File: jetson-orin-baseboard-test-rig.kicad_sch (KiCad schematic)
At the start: 18 parts, among them J1 PinHeader_2x6_P2.54mm_Drill1.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, J2 PinHeader_2x6_P2.54mm_Drill1.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, J3 PinHeader_2x6_P2.54mm_Drill1.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, J4 PinHeader_2x6_P2.54mm_Drill1.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, J5 PinHeader_2x6_P2.54mm_Drill1.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, J6 PinHeader_2x6_P2.54mm_Drill1.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, J7 PinHeader_2x6_P2.54mm_Drill1.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

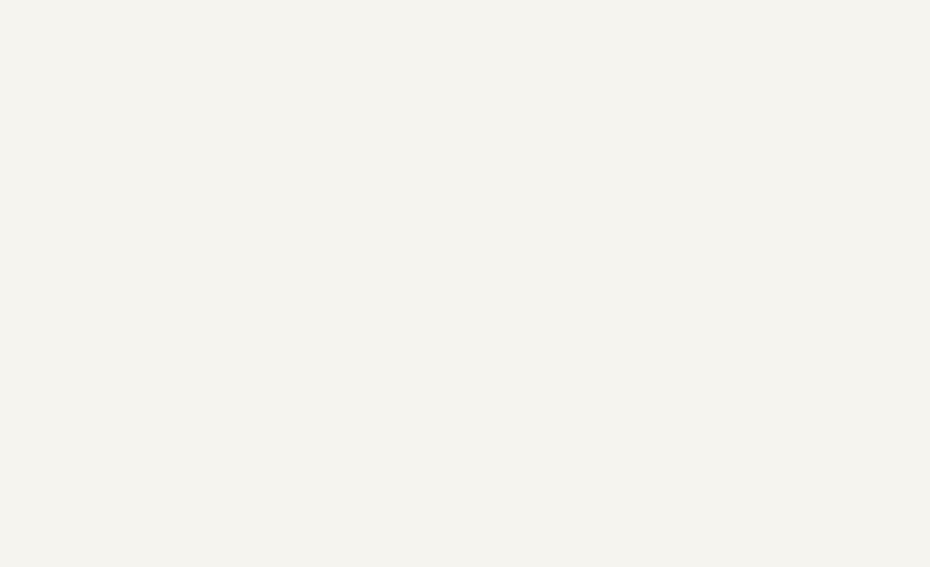
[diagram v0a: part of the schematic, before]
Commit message: [#77400] Add spring probes (WiP)
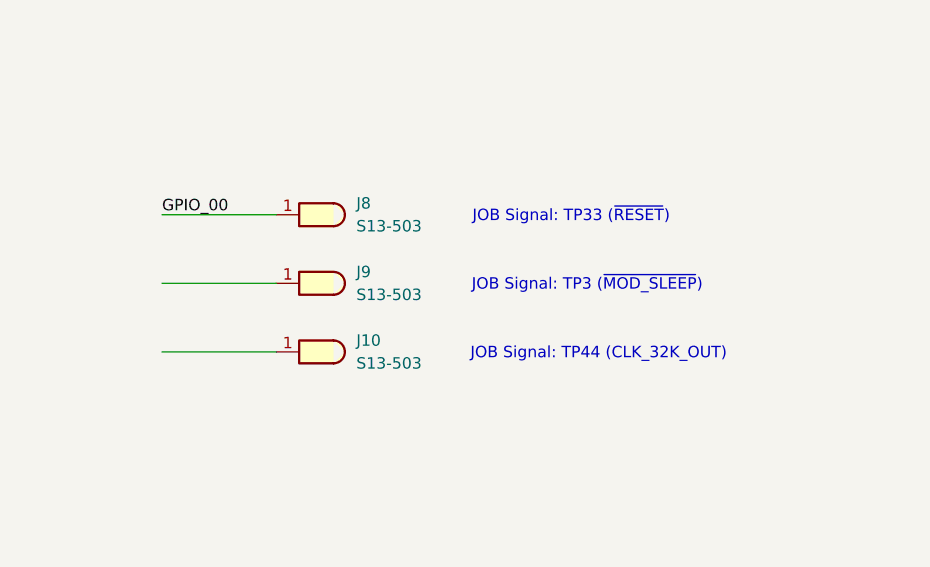
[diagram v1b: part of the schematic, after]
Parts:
- added J10, J8, J9: Harwin_1x1_H17.75mm_Drill0.8mm_S13-503, antmicro-footprints:PogoPin_Harwin_1x1_H17.75mm_Drill0.8mm_S13-503, symbol antmicroPogoPins:Harwin_1x1_H17.75mm_Drill0.8mm_S13-503
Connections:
- net GPIO_00: now also J8.1
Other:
- note added: "JOB Signal: TP3 (~{MOD_SLEEP})"
- note added: "JOB Signal: TP33 (~{RESET})"
- note added: "JOB Signal: TP44 (CLK_32K_OUT)"

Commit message: [#77400] Finalize schematic
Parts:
- added D1, D2: LED_G_0603_KP-1608CGCK, antmicro-footprints:LED_0603_1608Metric_G, symbol antmicroLEDIndicationDiscrete:LED_G_0603_KP-1608CGCK
- added J11, J12, J13, J14, J15, J16, J17, J18, J19, J20, J21, J22, J23, J24, J25, J26, J27, J28, J29, J30: Harwin_1x1_H17.75mm_Drill0.8mm_S13-503, antmicro-footprints:PogoPin_Harwin_1x1_H17.75mm_Drill0.8mm_S13-503, symbol antmicroPogoPins:Harwin_1x1_H17.75mm_Drill0.8mm_S13-503
- added Q1: BSS84, antmicro-footprints:SOT-23-3, symbol antmicroTransistorsFETsMOSFETsSingle:BSS84
- added R1: R_330R_0402, antmicro-footprints:R_0402_1005Metric, symbol antmicroResistors0402:R_330R_0402
- added R10, R11, R12, R18, R3, R5, R6, R7, R8, R9: R_0R_0402, antmicro-footprints:R_0402_1005Metric, symbol antmicroResistors0402:R_0R_0402
- added R13, R2: R_3k9_0402, antmicro-footprints:R_0402_1005Metric, symbol antmicroResistors0402:R_3k9_0402
- added R14, R15, R16, R17: R_68k_0402, antmicro-footprints:R_0402_1005Metric, symbol antmicroResistors0402:R_68k_0402
- added R19, R4: R_10k_0402, antmicro-footprints:R_0402_1005Metric, symbol antmicroResistors0402:R_10k_0402
- H3, H4, H5, H6: now not fitted; now left out of the parts list
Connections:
- net +3V3: now also D1.2 (A), Q1.2 (S), R19.2, R4.2
- net ADC_A_IN0: now also R17.1
- net ADC_A_IN1: now also R16.1
- net ADC_A_IN2: now also R15.1
- net ADC_A_IN3: now also R14.1
- net ADC_A_IN4: now also R13.2
- net ADC_A_IN5: now also R10.1
- net ADC_A_IN6: now also R11.1
- net ADC_A_IN7: now also R12.1
- net GND: now also J24.1, R1.1, R2.1
- net GPIO_00: now also R3.1; no longer J8.1
- net GPIO_01: now also R18.1, R19.1, R9.1
- net SPI_CS0: now also R5.1
- net SPI_MISO: now also R7.1
- net SPI_MOSI: now also R8.1
- net SPI_SCLK: now also R6.1
- net VCC: now also D2.2 (A)
- new net: J27.1, R6.2
- new net: D2.1 (C), R2.2
- new net: J23.1, R12.2
- new net: J19.1, R14.2
- new net: J22.1, R11.2
- new net: J21.1, R10.2
- new net: J18.1, R15.2
- new net: J28.1, R7.2
- new net: J16.1, R17.2
- new net: J20.1, R13.1
- new net: J8.1, R3.2
- new net: J25.1, Q1.3 (D)
- new net: D1.1 (C), R1.2
- new net: J26.1, R5.2
- new net: Q1.1 (G), R4.1, R9.2
- new net: J29.1, R8.2
- new net: J17.1, R16.2
- new net: J30.1, R18.2
- no-connect marks 0 -> 7
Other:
- note added: "Analog: 0-1.8V"
- note added: "Analog: 0-20V"
- note added: "Analog: 0-3.3V"
- note added: "Analog: 0-5V"
- note added: "Input on JOB (3V3): * Drive high to turn on +5V, +3V3 and +1V8 power rails * Keep HiZ otherwise"
- note added: "JOB Signal: J9-Pin1 (EEPROM_PWR)"
- note added: "JOB Signal: J9-Pin2 (~{CS})"
- note added: "JOB Signal: J9-Pin4 (SCK)"
- note added: "JOB Signal: J9-Pin6 (MISO)"
- note added: "JOB Signal: J9-Pin8 (MOSI)"
- note added: "JOB Signal: SP7-Pin1 (GND)"
- note added: "JOB Signal: TP1 (USBC3_VBUS)"
- note added: "JOB Signal: TP13 (U6-Pin30)"
- note added: "JOB Signal: TP14 (VCC)"
- note added: "JOB Signal: TP17 (USBC0_VBUS)"
- note added: "JOB Signal: TP22 (HDMI_HPD)"
- note added: "JOB Signal: TP23 (GND)"
- note added: "JOB Signal: TP29 (USBC1_VBUS)"
- note added: "JOB Signal: TP30 (USBC_HPD)"
- note added: "JOB Signal: TP31 (USBC1_DIR)"
- note added: "JOB Signal: TP32 (USBC1_FAULT_N)"
- note added: "JOB Signal: TP52 (3V3_STDB)"
- note added: "JOB Signal: TP53 (+5V)"
- note added: "JOB Signal: TP54 (+3V3)"
- note added: "JOB Signal: TP55 (+1V8)"
- note added: "Set to 0V to turn on EEPROM power Set to HiZ to turn off EEPROM power"
- note added: "This signal can be used to detect presence of the DUT * 0V - DUT is present * 3.3V - DUT is not present"
- moved on the sheet: C1, C2, C3, C4, C5, C6, C7, J1, J2, J3, J4, J5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

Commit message: [#77400] Clean ERC
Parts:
- J10, J11, J12, J13, J14, J15, J16, J17, J18, J19, J20, J21, J22, J23, J24, J25, J26, J27, J28, J29, J30, J8, J9: symbol antmicroPogoPins:Harwin_1x1_H17.75mm_Drill0.8mm_S13-503 -> antmicroPogoPins:Harwin_1x1_H17.75mm_Drill0.8mm_S13-503_CUSTOM
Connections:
- no-connect marks 7 -> 49

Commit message: [#77400] Finish routing
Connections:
- net ADC_A_IN1: now also R15.1; no longer R16.1
- net ADC_A_IN2: now also R13.2; no longer R15.1
- net ADC_A_IN3: now also R11.1; no longer R14.1
- net ADC_A_IN4: now also R16.1; no longer R13.2
- net ADC_A_IN5: now also R14.1; no longer R10.1
- net ADC_A_IN6: now also R10.1; no longer R11.1
- net GPIO_01: no longer R9.1
- net GPIO_02: now also R9.1
- net VCC: now also J19.1, R14.2
- no-connect marks 49 -> 48
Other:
- moved on the sheet: R10, R11, R12, R13, R14, R15, R16, R17

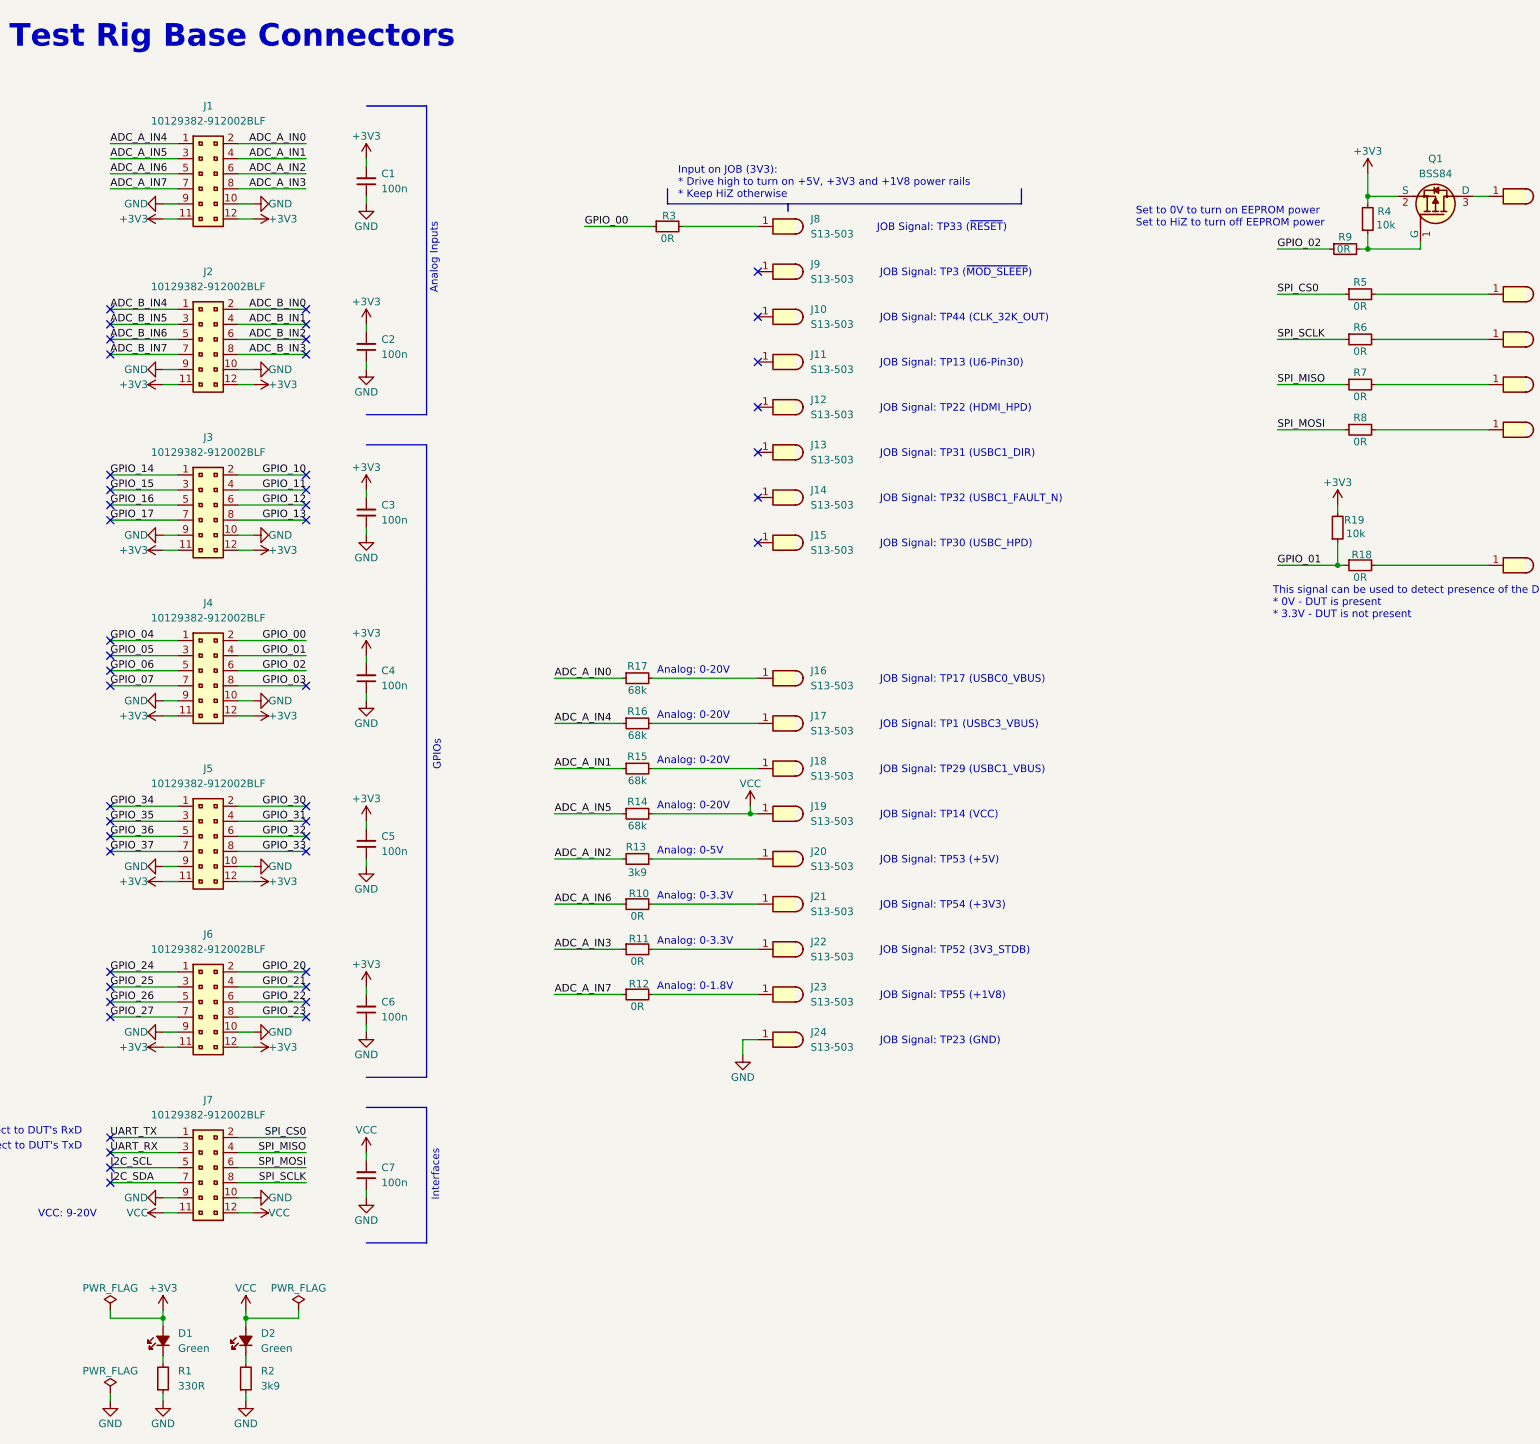
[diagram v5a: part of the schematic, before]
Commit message: [#77400] Add LEDs
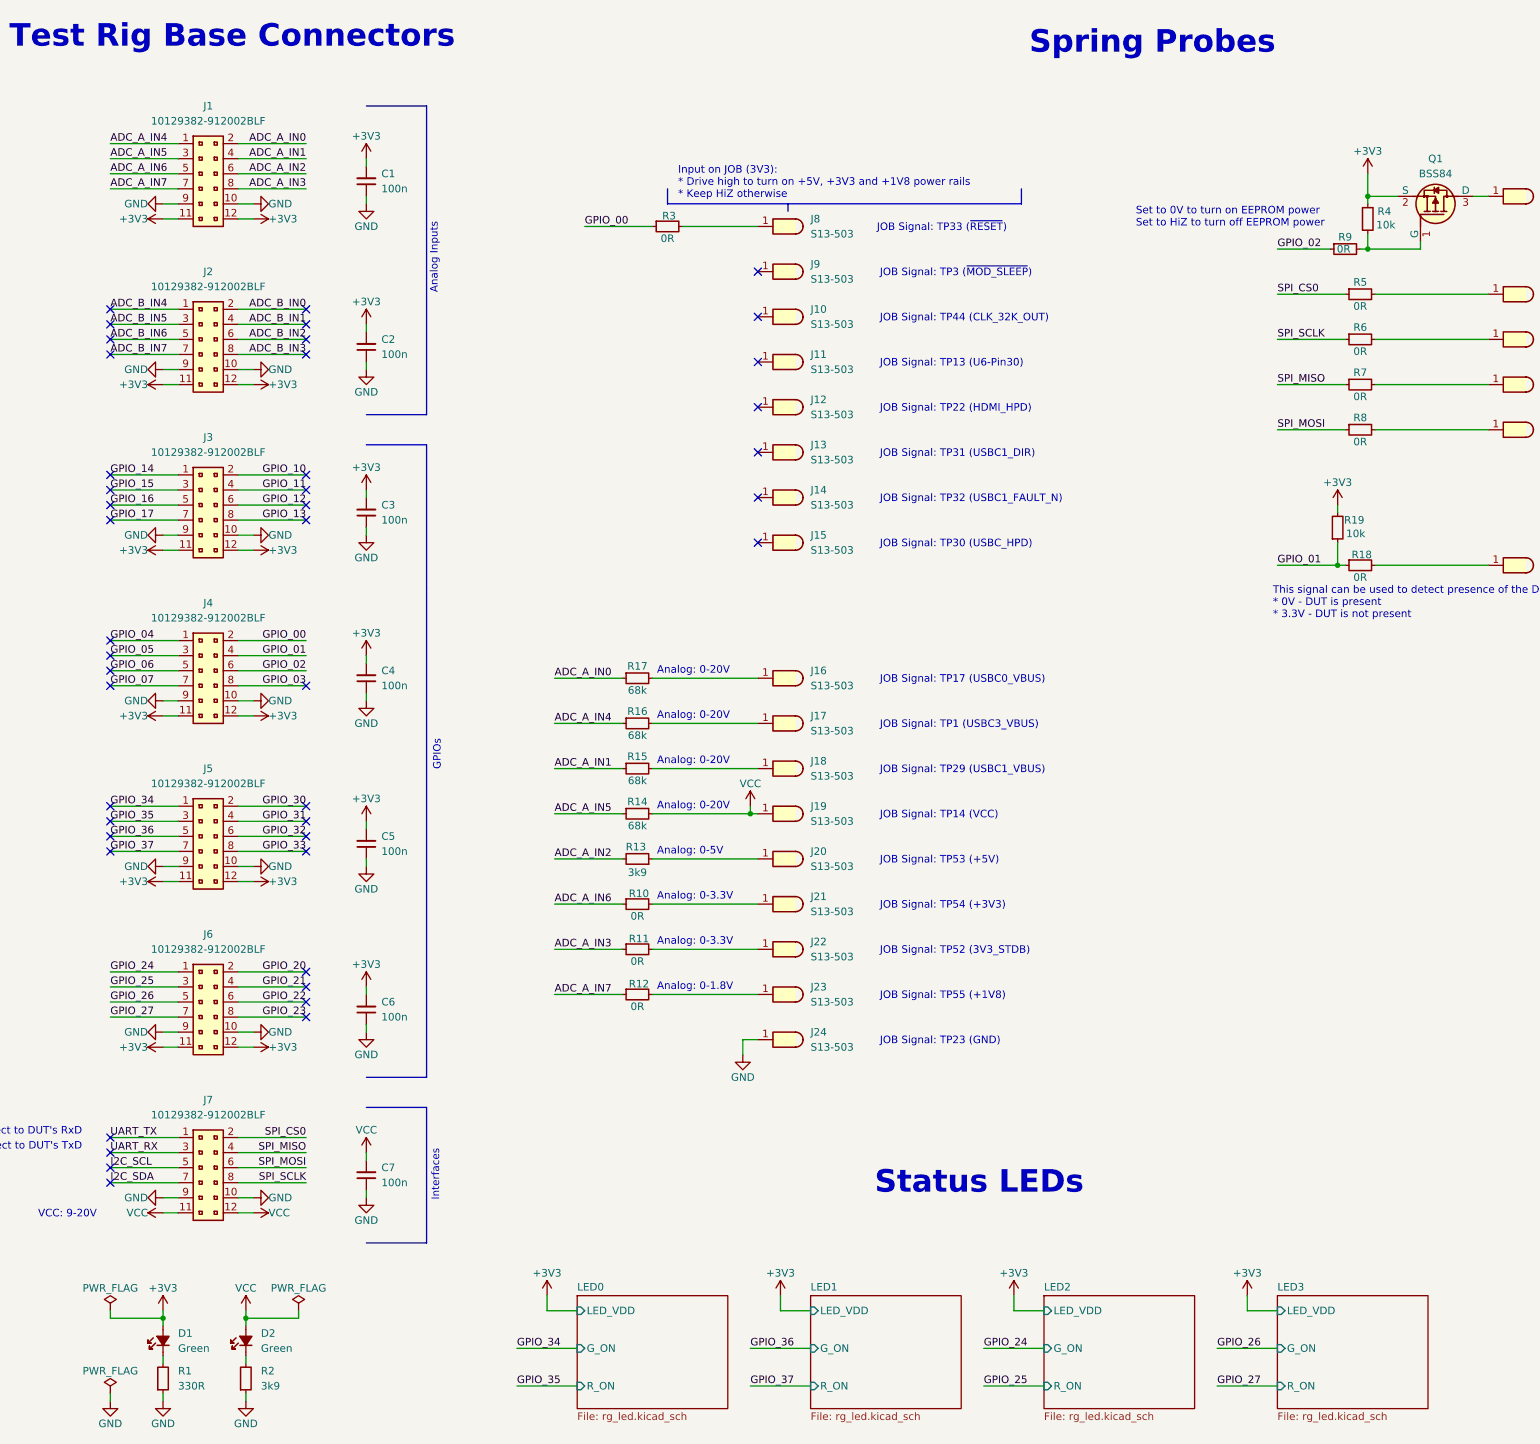
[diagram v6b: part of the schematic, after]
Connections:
- no-connect marks 48 -> 44
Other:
- added sheet LED0 (rg_led.kicad_sch)
- added sheet LED1 (rg_led.kicad_sch)
- added sheet LED2 (rg_led.kicad_sch)
- added sheet LED3 (rg_led.kicad_sch)
- note added: "Spring Probes"
- note added: "Status LEDs"

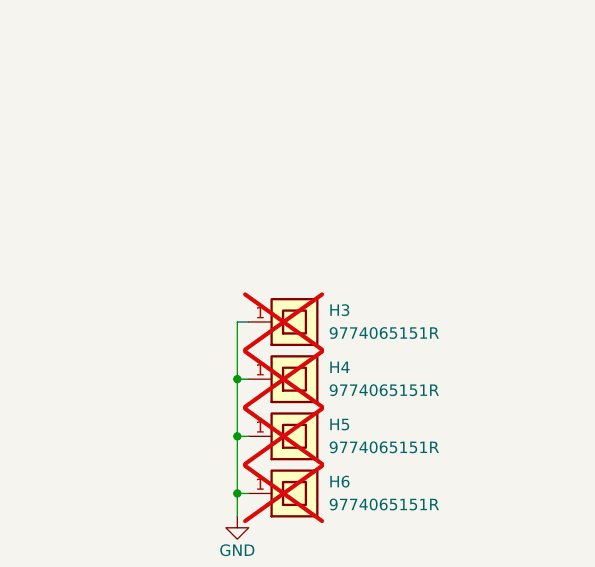
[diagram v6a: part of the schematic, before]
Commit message: [#77400] Add grounded mounting pad
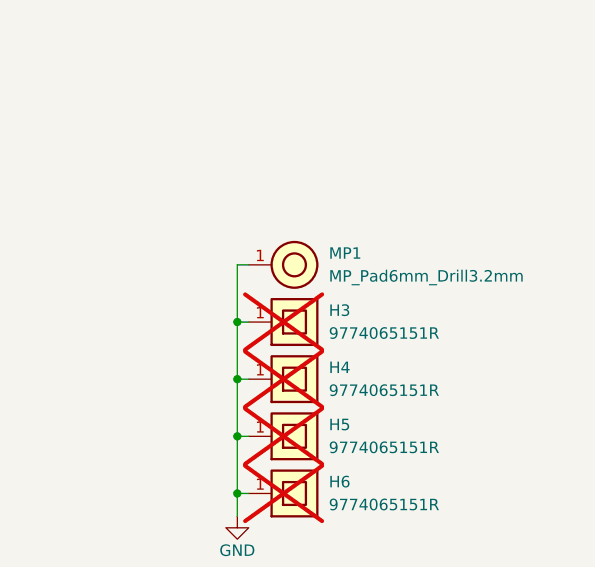
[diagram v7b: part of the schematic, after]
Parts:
- added MP1: MP_Pad6mm_Drill3.2mm, antmicro-footprints:MP_Pad6mm_Drill3.2mm, symbol antmicroMechanicalParts:MP_Pad6mm_Drill3.2mm
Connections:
- net GND: now also MP1.1
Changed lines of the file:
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@@
 	(title_block
 		(title "Jetson Orin Baseboard Test Rig")
-		(date "2025-05-16")
+		(date "2025-05-26")
 		(rev "1.0.0")
 		(company "Antmicro Ltd")
@@
 	)
 	(junction
+		(at 367.03 215.9)
+		(diameter 0)
+		(color 0 0 0 0)
+	)
+	(junction
 		(at 59.69 241.3)
 		(diameter 0)
@@
 	(wire
 		(pts
+			(xy 368.3 209.55) (xy 367.03 209.55)
+		)
+		(stroke
+			(width 0)
+			(type default)
+		)
+	)
+	(wire
+		(pts
 			(xy 203.2 240.03) (xy 203.2 237.49)
 		)
@@
 		)
 	)
+	(wire
+		(pts
+			(xy 367.03 209.55) (xy 367.03 215.9)
+		)
+		(stroke
+			(width 0)
+			(type default)
+		)
+	)
 	(polyline
 		(pts
@@
 					(unit 1)
 				)
+			)
+		)
+	)
+	(symbol
+		(lib_id "antmicroMechanicalParts:MP_Pad6mm_Drill3.2mm")
+		(at 368.3 209.55 0)
+		(unit 1)
+		(exclude_from_sim no)
+		(in_bom no)
+		(on_board yes)
+		(dnp no)
+		(fields_autoplaced yes)
+		(property "Reference" "MP1"
+			(at 377.19 208.28 0)
+			(effects
+				(font
+					(size 1.27 1.27)
+					(thickness 0.15)
+				)
+				(justify left)
+			)
+		)
+		(property "Value" "MP_Pad6mm_Drill3.2mm"
+			(at 377.19 210.82 0)
+			(effects
+				(font
+					(size 1.27 1.27)
+					(thickness 0.15)
+				)
+				(justify left)
+			)
+		)
+		(property "Footprint" "antmicro-footprints:MP_Pad6mm_Drill3.2mm"
+			(at 388.62 217.17 0)
+			(effects
+				(font
+					(size 1.27 1.27)
+					(thickness 0.15)
+				)
+				(justify left bottom)
+				(hide yes)
+			)
+		)
+		(property "Datasheet" ""
+			(at 385.14 225.12 0)
+			(effects
+				(font
+					(size 1.27 1.27)
+					(thickness 0.15)
+				)
+				(justify left bottom)
+				(hide yes)
+			)
+		)
+		(property "Description" "Mechanical part"
+			(at 368.3 209.55 0)
+			(effects
+				(font
+					(size 1.27 1.27)
+				)
+				(hide yes)
+			)
+		)
+		(property "Author" "Antmicro"
+			(at 388.62 219.71 0)
+			(effects
+				(font
+					(size 1.27 1.27)
+					(thickness 0.15)
+				)
+				(justify left bottom)
+				(hide yes)
+			)
+		)
+		(property "License" "Apache-2.0"
+			(at 388.62 222.25 0)
+			(effects
+				(font
+					(size 1.27 1.27)
+					(thickness 0.15)
+				)
+				(justify left bottom)
+				(hide yes)
+			)
+		)
+		(pin "1"
+		)
+		(instances
+			(project ""
+				(path "/4b393452-b11e-416e-bc83-918ae3cab2f1"
+					(reference "MP1")
+					(unit 1)
+				)
